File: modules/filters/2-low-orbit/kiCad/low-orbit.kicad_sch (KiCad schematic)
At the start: 94 parts, among them J1 IN, J2 CV_INPUT_1, J3 CV_INPUT_2, J4 PWR, J5 FILTER_OUT, Q1 BC548, U1 TL074, U2 TL074

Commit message: update components, PCB 3320 and design
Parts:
- removed C1, C15: C_1uF (MKS), Synth:C_RECT_MKT_1uF, symbol synth:C_1uF (MKS)
- removed CUTOFF1, RES_AMOUNT1: B100K, Synth:Potentiometer_TT_P0915N, symbol synth:R_Potentiometer (P0915N)
- removed CV_CTL_IN_1, CV_CTL_IN_2, INPUT_LVL1: B100K, Synth:Potentiometer_Alpha_RD901F-40-00D_Single_Vertical_CircularHoles, symbol synth:R_Potentiometer (Alpha_9mm)
- removed D1: LED, LED_THT:LED_D3.0mm, symbol Device:LED
- removed D11, D12, D2: 1N4148, Synth:D_DO-35_SOD27_P7.62mm_Horizontal, symbol synth:D_Signal (1N4148)
- removed H1: TOP_4_SGL, Synth:PinHeader_1x04_P2.54mm_Vertical, symbol synth:PinHeader_01x04
- removed H2: BTM_4_SGL, Synth:PinSocket_1x04_P2.54mm_Vertical, symbol synth:PinSocket_01x04
- removed unit 1 of H3
- removed unit 2 of H3
- removed unit 2 of H4
- removed unit 1 of H4
- removed J1: IN, Synth:Jack_3.5mm_QingPu_WQP-PJ398SM_Vertical_CircularHoles, symbol synth:AudioJack_Mono_3.5mm
- removed J2: CV_INPUT_1, Synth:Jack_3.5mm_QingPu_WQP-PJ398SM_Vertical_CircularHoles, symbol synth:AudioJack_Mono_3.5mm
- removed J3: CV_INPUT_2, Synth:Jack_3.5mm_QingPu_WQP-PJ398SM_Vertical_CircularHoles, symbol synth:AudioJack_Mono_3.5mm
- removed J5: FILTER_OUT, Synth:Jack_3.5mm_QingPu_WQP-PJ398SM_Vertical_CircularHoles, symbol synth:AudioJack_Mono_3.5mm
- removed Q1: BC548, Package_TO_SOT_THT:TO-92_HandSolder, symbol Transistor_BJT:BC548
- removed R2, R21, R25, R3: 100K [1%], Synth:R_Default (DIN0207), symbol synth:R_Default
- removed R22, R24, R26: 1K [1%], Synth:R_Default (DIN0207), symbol synth:R_Default
- removed R23: 33K [1%], Synth:R_Default (DIN0207), symbol synth:R_Default
- removed R4, R5: 68K [1%], Synth:R_Default (DIN0207), symbol synth:R_Default
- removed R6: 2K [1%], Synth:R_Default (DIN0207), symbol synth:R_Default
- removed R7: 470, Synth:R_Default (DIN0207), symbol synth:R_Default
- removed R8: 14K [1%], Synth:R_Default (DIN0207), symbol synth:R_Default
- removed RES_INT1: B50K, Synth:Potentiometer_TT_P0915N, symbol synth:R_Potentiometer (P0915N)
- removed TP1: INPUT, Connector_Pin:Pin_D1.0mm_L10.0mm, symbol Connector:TestPoint
- removed TP10: RES_AMT, Connector_Pin:Pin_D1.0mm_L10.0mm, symbol Connector:TestPoint
- removed TP11: PRE_OUT, Connector_Pin:Pin_D1.0mm_L10.0mm, symbol Connector:TestPoint
- removed TP12: OUT, Connector_Pin:Pin_D1.0mm_L10.0mm, symbol Connector:TestPoint
- removed TP2: CUTOFF, Connector_Pin:Pin_D1.0mm_L10.0mm, symbol Connector:TestPoint
- removed TP3: CUTOFF_BUFF, Connector_Pin:Pin_D1.0mm_L10.0mm, symbol Connector:TestPoint
- removed TP9: FILTER_OUT, Connector_Pin:Pin_D1.0mm_L10.0mm, symbol Connector:TestPoint
- removed unit 4 of U1
- removed unit 3 of U1
- removed unit 2 of U1
- removed unit 1 of U2
- removed unit 2 of U2
- added BAND_PASS_1: BAND_PASS, Synth:SW_default, symbol synth:SW_SPDT
- added D1: LED, Synth:LED_D5.0mm (center Aligned), symbol synth:LED (5mm)
- added H1: PinHeader_01x04, Synth:PinSocket_1x04_P2.54mm_Vertical, symbol synth:PinSocket_01x04
- added H2: PinSocket_01x04, Synth:PinHeader_1x04_P2.54mm_Vertical, symbol synth:PinHeader_01x04
- added H4: BTM_4_SGL, Synth:PinSocket_1x04_P2.54mm_Vertical, symbol synth:PinSocket_01x04
- added H5: TOP_4_SGL, Synth:PinHeader_1x04_P2.54mm_Vertical, symbol synth:PinHeader_01x04
- added HIGH_PASS_1: HIGH_PASS, Synth:SW_default, symbol synth:SW_SPDT
- added LOW_PASS_1: LOW_PASS, Synth:SW_default, symbol synth:SW_SPDT
- R1: value 27K [1%] -> 470
- R11: renamed from R17; value 10 -> 10R
- R12: renamed from R18; value 10 -> 10R
- R13: renamed from R20; value 2K [1%] -> 2K
- R2: renamed from R9; value 100K [1%] -> 100K
- R4: renamed from R11; value 27K [1%] -> 27K
- TP8: value RES_INTENSITY -> FILTER_OUT
- renumbered C2 to C1, C11 to C10, C12 to C11, C13 to C12, C14 to C13, C3 to C2, C4 to C3, C5 to C4, C6 to C5, C7 to C6, C8 to C7, C9 to C8, C10 to C9, D3 to D2, D4 to D3, D5 to D4, D6 to D5, D7 to D6, D8 to D7, D9 to D8, D10 to D9, H8 to H10, H9 to H11, H10 to H12, H11 to H13, H12 to H14, H4 to H6, H5 to H7, H6 to H8, H7 to H9, J4 to J1, R19 to R10, R10 to R3, R12 to R5, R13 to R6, R14 to R7, R15 to R8, R16 to R9, TP4 to TP1, TP13 to TP2, TP15 to TP3, TP14 to TP4
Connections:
- net +12V: now also R1.1
- net -12V: no longer H3.8 (Pin_8), H6.8 (Pin_8), R1.2
- net GNDREF: now also H3.8 (Pin_8), H6.8 (Pin_8), BAND_PASS_1.1 (A), D1.1 (K), H4.3 (Pin_3), H5.3 (Pin_3), HIGH_PASS_1.1 (A), LOW_PASS_1.1 (A); no longer C10.1, C11.1, C12.1
- net output/input: now reaches TP8.1
- net output/input: now also H6.3 (Pin_3), U1.1, U1.2 (-)
- net resonance/output: now reaches C13.1, C9.1, TP5.1
- net cv-input/cv_out: now reaches R2.1, R3.2, R4.2, R6.1, TP1.1
- net resonance/input: now reaches H3.3 (Pin_3)
- net at R7.1, R8.1: now also H1.4 (Pin_4)
- new net: BAND_PASS_1.3 (C), H2.1 (Pin_1), HIGH_PASS_1.3 (C), LOW_PASS_1.3 (C)
- new net: D1.2 (A), R1.2
- new net: C10.1, C12.1, H1.3 (Pin_3)
- new net: C11.1, H1.2 (Pin_2)
- new net: BAND_PASS_1.2 (B), H2.3 (Pin_3)
- new net: H2.4 (Pin_4), LOW_PASS_1.2 (B)
- new net: H2.2 (Pin_2), HIGH_PASS_1.2 (B)
- new net input/output: H1.1 (Pin_1)
- no-connect marks 1 -> 0
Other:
- added sheet cv-input (cv-input.kicad_sch)
- added sheet input (input.kicad_sch)
- added sheet output (output.kicad_sch)
- added sheet resonance (resonance.kicad_sch)
- note removed: "As long as these are high inputs (buffered) we can drive the LED?"
- note removed: "Cutoff"
- note removed: "LED conn point"
- note removed: "RES Amount"
- note removed: "RES Intensity"
- moved on the sheet: C10, C11, C12, C13, C9, D4, D5, D6, D7, D8, D9, H3C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

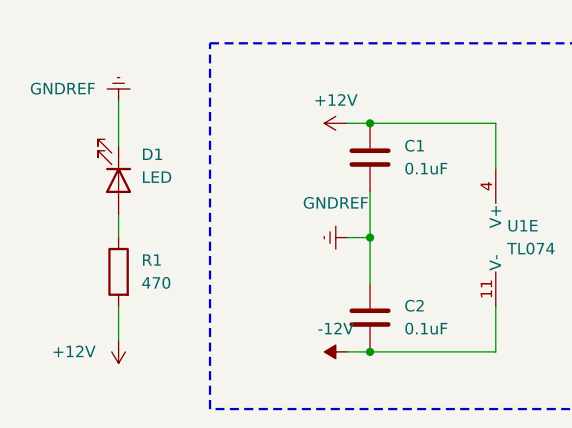
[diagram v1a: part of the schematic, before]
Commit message: update component status, add IBOM for built modules
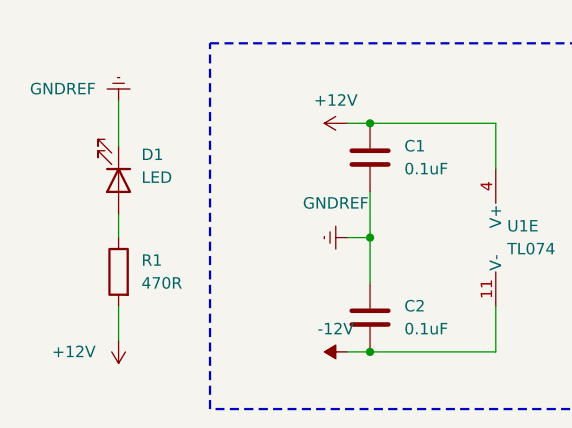
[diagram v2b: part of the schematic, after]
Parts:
- H1: value PinHeader_01x04 -> PinSocket_01x04
- H2: value PinSocket_01x04 -> PinHeader_01x04
- H3: value TOP_8_SGL -> PinHeader_01x08
- H4: value BTM_4_SGL -> PinSocket_01x04
- H5: value TOP_4_SGL -> PinHeader_01x04
- H6: value BTM_8_SGL -> PinSocket_01x08
- R1: value 470 -> 470R
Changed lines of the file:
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@@
 			)
 		)
-		(property "Value" "PinSocket_01x04"
+		(property "Value" "PinHeader_01x04"
 			(at 111.76 46.9901 0)
 			(effects
@@
 			)
 		)
-		(property "Value" "TOP_8_SGL"
+		(property "Value" "PinHeader_01x08"
 			(at 267.97 266.7 0)
 			(effects
@@
 			)
 		)
-		(property "Value" "BTM_8_SGL"
+		(property "Value" "PinSocket_01x08"
 			(at 280.67 274.32 0)
 			(effects
@@
 			)
 		)
-		(property "Value" "BTM_8_SGL"
+		(property "Value" "PinSocket_01x08"
 			(at 280.67 281.94 0)
 			(effects
@@
 			)
 		)
-		(property "Value" "PinSocket_01x04"
+		(property "Value" "PinHeader_01x04"
 			(at 208.28 130.8099 0)
 			(effects
@@
 			)
 		)
-		(property "Value" "TOP_8_SGL"
+		(property "Value" "PinHeader_01x08"
 			(at 267.97 269.24 0)
 			(effects
@@
 			)
 		)
-		(property "Value" "BTM_8_SGL"
+		(property "Value" "PinSocket_01x08"
 			(at 280.67 271.78 0)
 			(effects
@@
 			)
 		)
-		(property "Value" "BTM_8_SGL"
+		(property "Value" "PinSocket_01x08"
 			(at 285.75 115.57 0)
 			(effects
@@
 			)
 		)
-		(property "Value" "PinHeader_01x04"
+		(property "Value" "PinSocket_01x04"
 			(at 207.01 128.2701 0)
 			(effects
@@
 			)
 		)
-		(property "Value" "TOP_8_SGL"
+		(property "Value" "PinHeader_01x08"
 			(at 290.83 111.76 0)
 			(effects
@@
 			)
 		)
-		(property "Value" "PinHeader_01x04"
+		(property "Value" "PinSocket_01x04"
 			(at 113.03 49.5299 0)
 			(effects
@@
 			)
 		)
-		(property "Value" "PinSocket_01x04"
+		(property "Value" "PinHeader_01x04"
 			(at 148.5901 69.85 0)
 			(effects
@@
 			)
 		)
-		(property "Value" "TOP_8_SGL"
+		(property "Value" "PinHeader_01x08"
 			(at 267.97 271.78 0)
 			(effects
@@
 			)
 		)
-		(property "Value" "PinHeader_01x04"
+		(property "Value" "PinSocket_01x04"
 			(at 207.01 140.9701 0)
 			(effects
@@
 			)
 		)
-		(property "Value" "470"
+		(property "Value" "470R"
 			(at 57.15 269.2399 0)
 			(effects
@@
 			)
 		)
-		(property "Value" "TOP_4_SGL"
+		(property "Value" "PinHeader_01x04"
 			(at 276.86 261.62 0)
 			(effects
@@
 			)
 		)
-		(property "Value" "BTM_8_SGL"
+		(property "Value" "PinSocket_01x08"
 			(at 280.67 276.86 0)
 			(effects
@@
 			)
 		)
-		(property "Value" "TOP_8_SGL"
+		(property "Value" "PinHeader_01x08"
 			(at 267.97 274.32 0)
 			(effects
@@
 			)
 		)
-		(property "Value" "TOP_8_SGL"
+		(property "Value" "PinHeader_01x08"
 			(at 267.97 276.86 0)
 			(effects
@@
 			)
 		)
-		(property "Value" "PinHeader_01x04"
+		(property "Value" "PinSocket_01x04"
 			(at 151.1299 68.58 0)
 			(effects
@@
 			)
 		)
-		(property "Value" "BTM_4_SGL"
+		(property "Value" "PinSocket_01x04"
 			(at 264.16 256.54 0)
 			(effects
@@
 			)
 		)
-		(property "Value" "PinSocket_01x04"
+		(property "Value" "PinHeader_01x04"
 			(at 208.28 143.5099 0)
 			(effects
@@
 			)
 		)
-		(property "Value" "BTM_8_SGL"
+		(property "Value" "PinSocket_01x08"
 			(at 280.67 279.4 0)
 			(effects
